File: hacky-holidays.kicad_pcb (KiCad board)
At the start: 2 copper layers, 96 x 96 mm, 39 parts, among them Q1 AO3401A, Q2 AO3400A, Q3 AO3400A, SW1 SW_Push, SW2 SW_Push, SW3 SW_Push, SW4 SW_SPDT, U1 TP4057, U2 CH552G, U3 DW01A

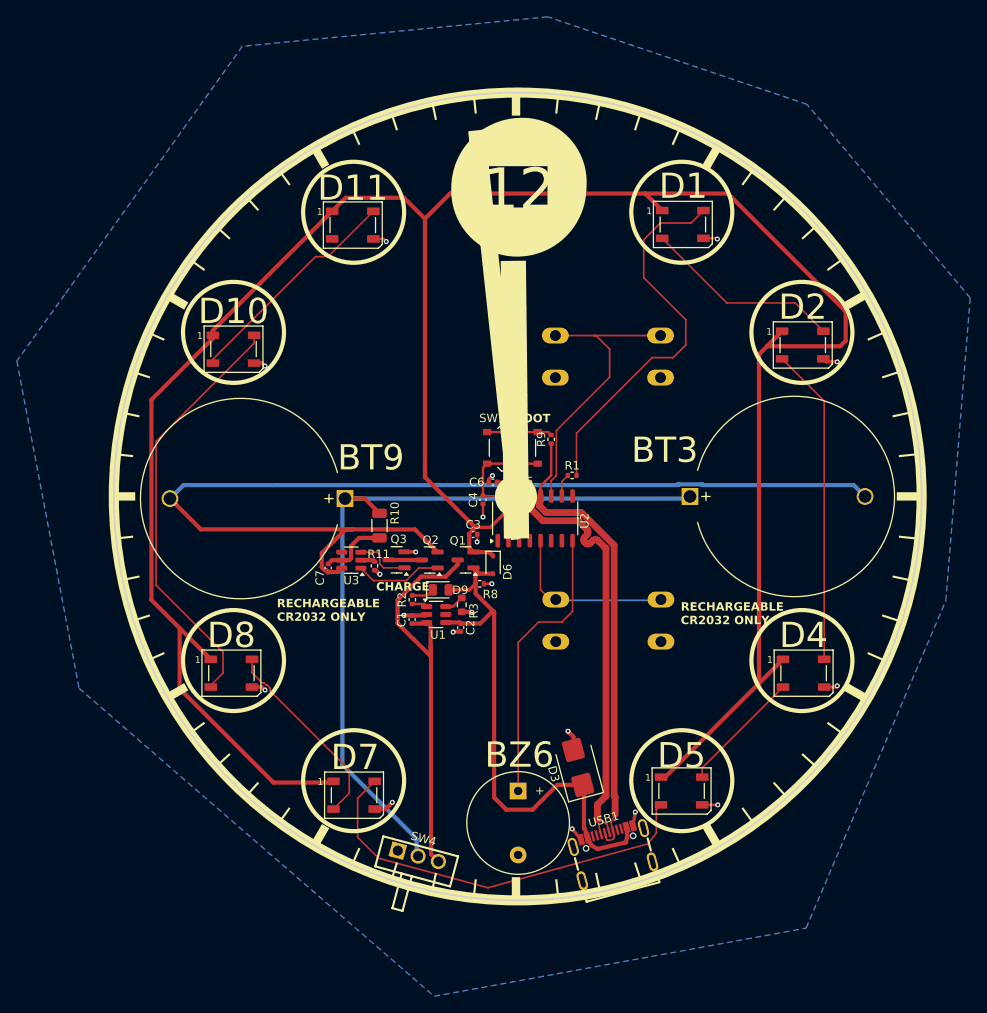
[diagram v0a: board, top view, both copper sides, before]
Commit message: update capacitor part numbers, add test pins, silkscreen updates
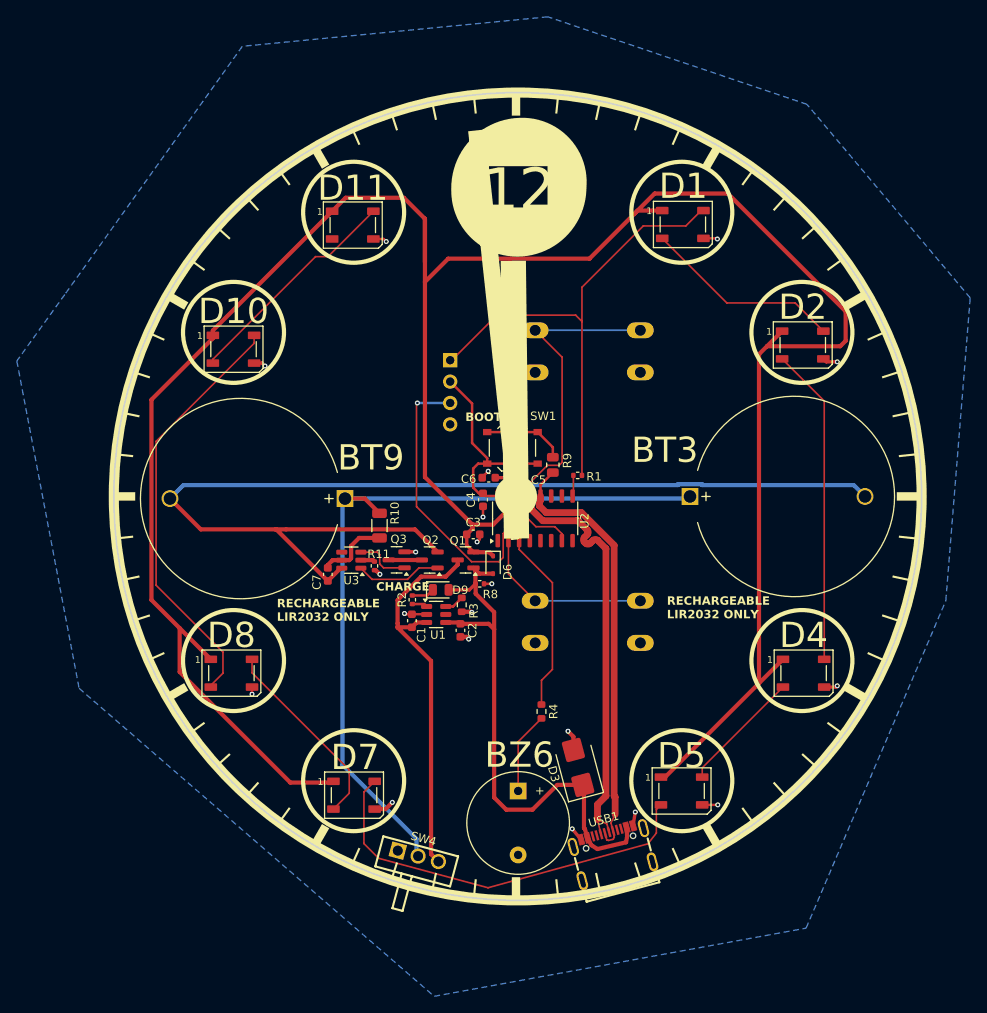
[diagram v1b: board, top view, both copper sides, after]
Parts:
- added J1: Conn_01x04_Pin, Connector_PinHeader_2.54mm:PinHeader_1x04_P2.54mm_Vertical, B.Cu at (199.0, 58.3)
- added QR*****: https://github.com/grimsteel/pixel-clock, custom-footprints:qrcode, B.Cu at (176.4, 75.0)
- added R4: 220, Resistor_SMD:R_0603_1608Metric, F.Cu at (209.8, 100.0)
- C1, C2, C3, C4, C5, C6, C7: footprint Capacitor_SMD:C_0402_1005Metric -> Capacitor_SMD:C_0603_1608Metric
- R9: footprint Resistor_SMD:R_0402_1005Metric -> Resistor_SMD:R_0805_2012Metric
- moved R9 3.05 mm to (211.2, 70.8)
- moved SW2 2.48 mm to (221.6, 54.8)
- moved SW3 2.45 mm to (221.6, 86.9)
- moved C7 0.77 mm to (184.5, 83.8)
- moved C6 0.73 mm to (203.6, 72.3)
- moved C5 0.71 mm to (206.6, 72.3)
- moved R1 0.65 mm to (214.2, 72.0)
- moved C2 0.34 mm to (200.2, 90.4)
- moved C1 0.15 mm to (194.4, 89.3)
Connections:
- BZ6 pad 1: BUZ -> Net-(BZ6-+)
- D1 pad 4: Net-(D1-DIN) -> WS2812B
- R1 pad 1: WS2812B -> Net-(U2-P1.1/T2EX/CAP2/TIN1/VBUS2/AIN0)
- R1 pad 2: Net-(D1-DIN) -> WS2812B
- U2 pad 10: WS2812B -> unconnected-(U2-P3.3/INT1-Pad10)
- U2 pad 11: BTN1 -> unconnected-(U2-P3.4/PWM2/RXD1_/T0-Pad11)
- U2 pad 2: unconnected-(U2-P1.4/T2_/CAP1_/SCS/TIN2/UCC1/AIN1-Pad2) -> BTN2
- U2 pad 3: unconnected-(U2-P1.5/MOSI/PWM1/TIN3/UCC2/AIN2-Pad3) -> BUZ
- U2 pad 5: BTN2 -> unconnected-(U2-P1.7/SCK/TXD1/TIN5-Pad5)
- U2 pad 7: unconnected-(U2-P3.1/PWM2_/TXD-Pad7) -> BTN1
- U2 pad 8: BUZ -> unconnected-(U2-P3.0/PWM1_/RXD-Pad8)
- U2 pad 9: unconnected-(U2-P1.1/T2EX/CAP2/TIN1/VBUS2/AIN0-Pad9) -> Net-(U2-P1.1/T2EX/CAP2/TIN1/VBUS2/AIN0)
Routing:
- net WS2812B: track 2.75 -> 58.7 mm
- net Net-(D1-DIN): track 45.5 -> 0.00 mm
- net BUZ: track 34.1 -> 56.9 mm, vias 0 -> 1
- net +3.3V: track 11.8 -> 25.1 mm
- net BTN1: track 35.4 -> 46.4 mm
- net Net-(BZ6-+): track 0.00 -> 9.77 mm
- net +5V: track 299.2 -> 307.9 mm
- net BATT: track 49.7 -> 46.2 mm
- net D+: track 55.6 -> 52.2 mm
- net Net-(U2-P1.1/T2EX/CAP2/TIN1/VBUS2/AIN0): track 0.00 -> 2.49 mm
- net Net-(R9-Pad2): track 7.74 -> 9.55 mm
- net -BATT: track 127.7 -> 129.5 mm
- net GND: track 34.3 -> 33.2 mm, vias 21 -> 22
- net VBUS: track 68.1 -> 67.1 mm
- net BTN2: track 20.1 -> 21.0 mm
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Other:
- board text added: "+3.3V"
- board text added: "BUZ"
- board text added: "GND"
- board text added: "NEO"
- board text added: "RECHARGEABLE LIR2032 ONLY"
- board text added: "github.com/grimsteel/pixel-clock"
- board text removed: "RECHARGEABLE CR2032 ONLY"

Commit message: tidy schematic
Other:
- board text added: "JLCJLCJLCJLC"
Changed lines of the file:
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@@
 		)
 		(property "Footprint" ""
-			(at 0 0 0)
-			(layer "B.Fab")
+			(at 0 0 180)
+			(layer "F.Fab")
 			(hide yes)
 			(effects
@@
 					(thickness 0.15)
 				)
-				(justify mirror)
 			)
 		)
@@
 		)
 	)
+	(gr_text "JLCJLCJLCJLC"
+		(at 227.37 83.85 0)
+		(layer "B.SilkS")
+		(effects
+			(font
+				(size 1 1)
+				(thickness 0.15)
+			)
+			(justify mirror)
+		)
+	)

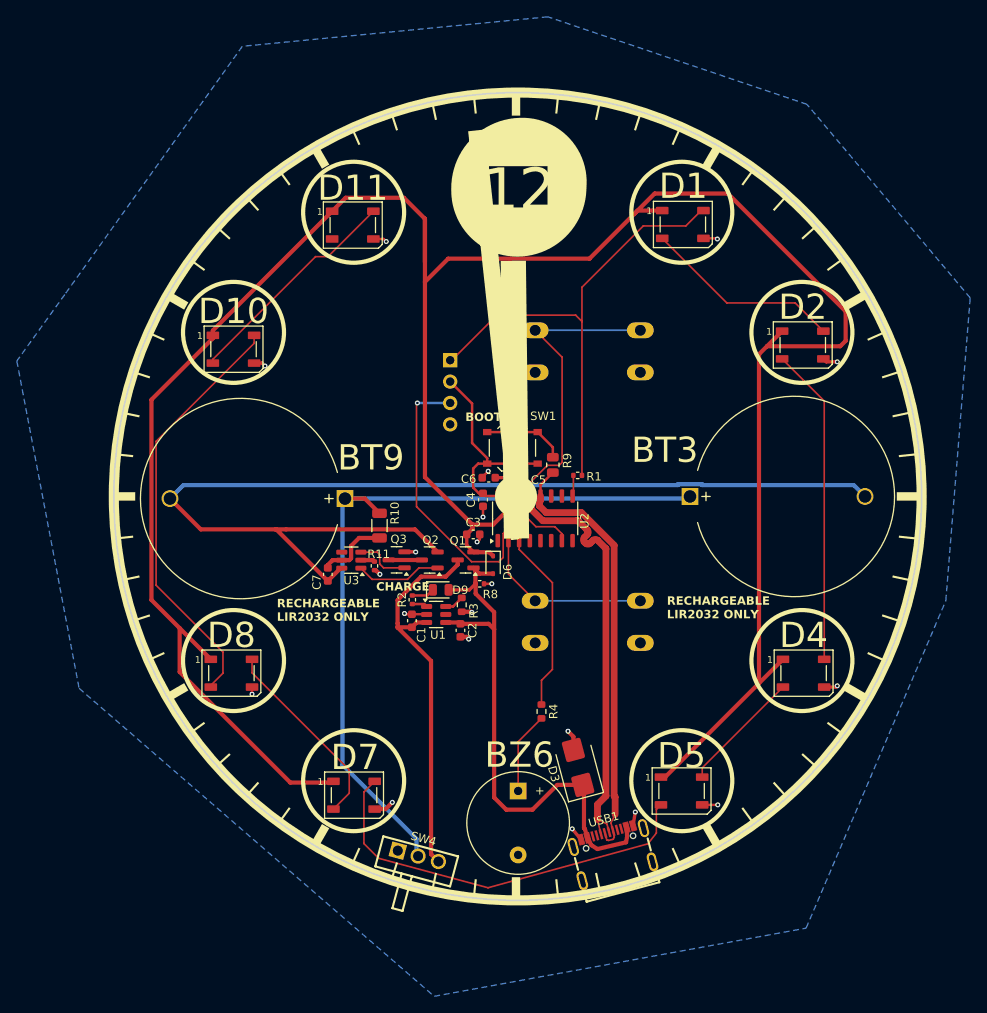
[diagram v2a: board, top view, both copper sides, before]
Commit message: add mounting hole
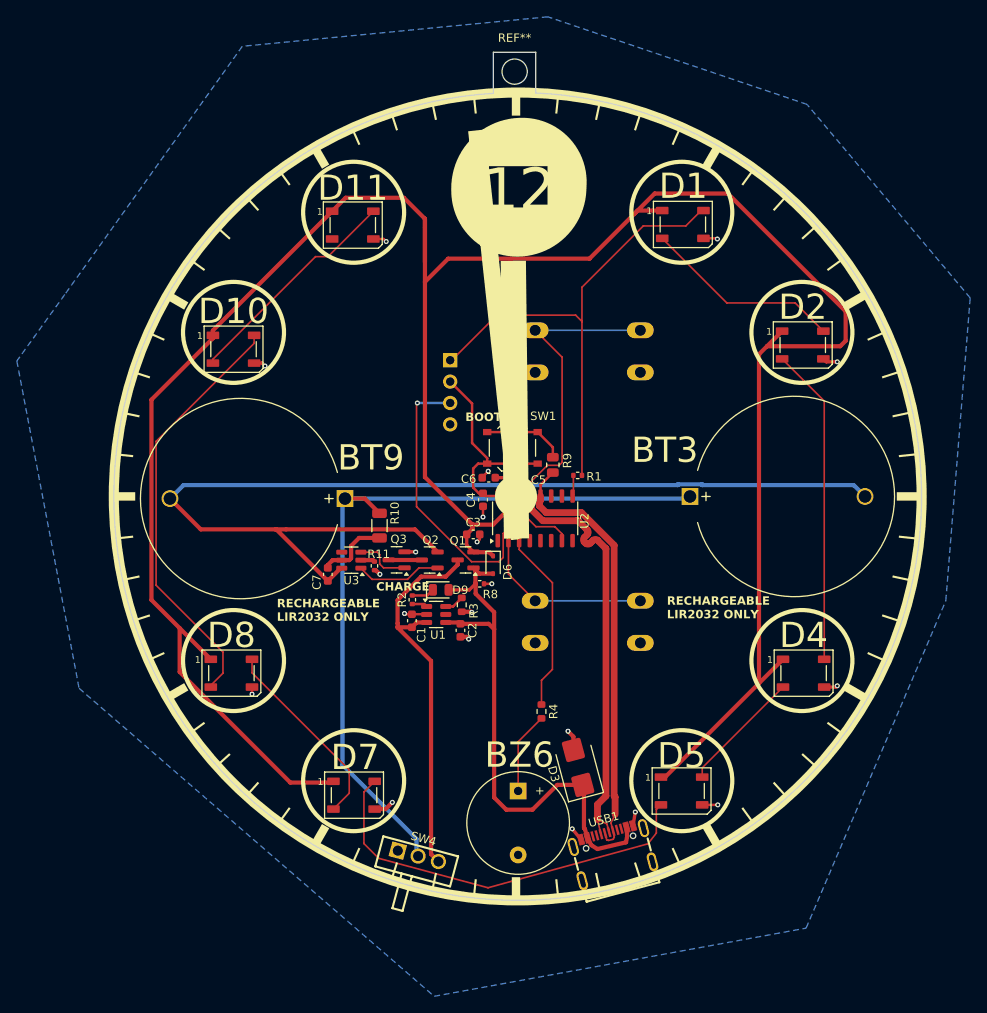
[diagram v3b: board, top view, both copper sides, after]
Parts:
- added REF**: MountingHole_3mm, MountingHole:MountingHole_3mm, F.Cu at (206.7, 24.0)
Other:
- board size 96 x 96 mm -> 96 x 100.8 mm
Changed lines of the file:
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@@
 		)
 	)
+	(footprint "MountingHole:MountingHole_3mm"
+		(layer "F.Cu")
+		(at 206.66 24.01)
+		(descr "Mounting Hole 3mm, no annular")
+		(tags "mounting hole 3mm no annular")
+		(property "Reference" "REF**"
+			(at 0 -4 0)
+			(layer "F.SilkS")
+			(effects
+				(font
+					(size 1 1)
+					(thickness 0.15)
+				)
+			)
+		)
+		(property "Value" "MountingHole_3mm"
+			(at 0 4 0)
+			(layer "F.Fab")
+			(effects
+				(font
+					(size 1 1)
+					(thickness 0.15)
+				)
+			)
+		)
+		(property "Footprint" ""
+			(at 0 0 0)
+			(layer "F.Fab")
+			(hide yes)
+			(effects
+				(font
+					(size 1.27 1.27)
+					(thickness 0.15)
+				)
+			)
+		)
+		(property "Datasheet" ""
+			(at 0 0 0)
+			(unlocked yes)
+			(layer "F.Fab")
+			(hide yes)
+			(effects
+				(font
+					(size 1.27 1.27)
+					(thickness 0.15)
+				)
+			)
+		)
+		(property "Description" ""
+			(at 0 0 0)
+			(unlocked yes)
+			(layer "F.Fab")
+			(hide yes)
+			(effects
+				(font
+					(size 1.27 1.27)
+					(thickness 0.15)
+				)
+			)
+		)
+		(attr exclude_from_pos_files exclude_from_bom)
+		(fp_circle
+			(center 0 0)
+			(end 3 0)
+			(stroke
+				(width 0.15)
+				(type solid)
+			)
+			(fill no)
+			(layer "Cmts.User")
+		)
+		(fp_circle
+			(center 0 0)
+			(end 3.25 0)
+			(stroke
+				(width 0.05)
+				(type solid)
+			)
+			(fill no)
+			(layer "F.CrtYd")
+		)
+		(fp_text user "${REFERENCE}"
+			(at 0 0 0)
+			(layer "F.Fab")
+			(effects
+				(font
+					(size 1 1)
+					(thickness 0.15)
+				)
+			)
+		)
+		(pad "" np_thru_hole circle
+			(at 0 0)
+			(size 3 3)
+			(drill 3)
+			(layers "*.Cu" "*.Mask")
+		)
+		(embedded_fonts no)
+	)
 	(footprint "LED_SMD:LED_WS2812B_PLCC4_5.0x5.0mm_P3.2mm"
 		(layer "F.Cu")
@@
 		(layer "Dwgs.User")
 	)
-	(gr_circle
-		(center 207.024991 74.5)
-		(end 255.024991 74.5)
+	(gr_line
+		(start 209.17 21.71)
+		(end 204.13 21.71)
 		(stroke
-			(width 0.2)
+			(width 0.05)
+			(type default)
+		)
+		(layer "Edge.Cuts")
+	)
+	(gr_line
+		(start 204.13 26.59)
+		(end 204.13 21.71)
+		(stroke
+			(width 0.05)
+			(type default)
+		)
+		(layer "Edge.Cuts")
+	)
+	(gr_arc
+		(start 209.168876 26.550518)
+		(mid 207.401062 122.495913)
+		(end 204.13 26.59)
+		(stroke
+			(width 0.05)
+			(type default)
+		)
+		(layer "Edge.Cuts")
+	)
+	(gr_line
+		(start 209.17 26.55)
+		(end 209.17 21.71)
+		(stroke
+			(width 0.05)
 			(type default)
 		)
-		(fill no)
 		(layer "Edge.Cuts")
 	)

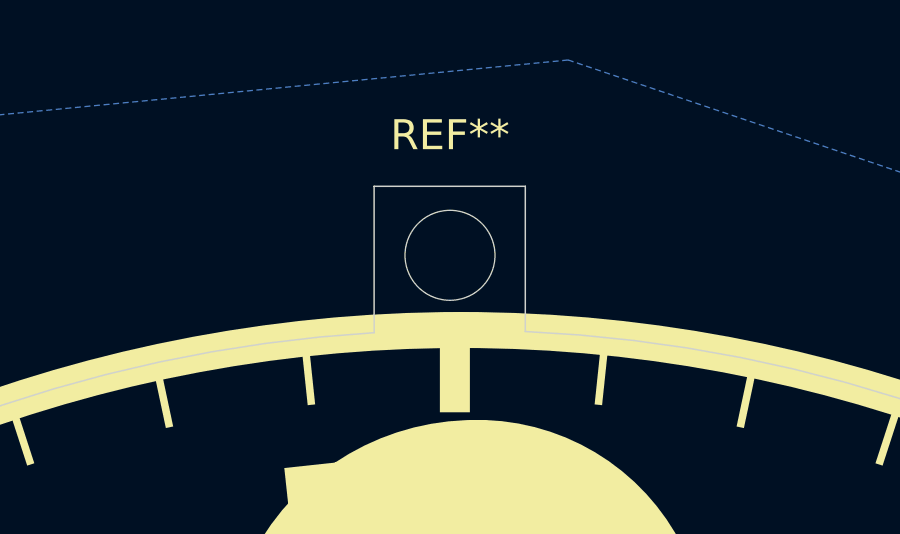
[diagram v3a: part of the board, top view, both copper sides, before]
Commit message: make pcb below 100x100
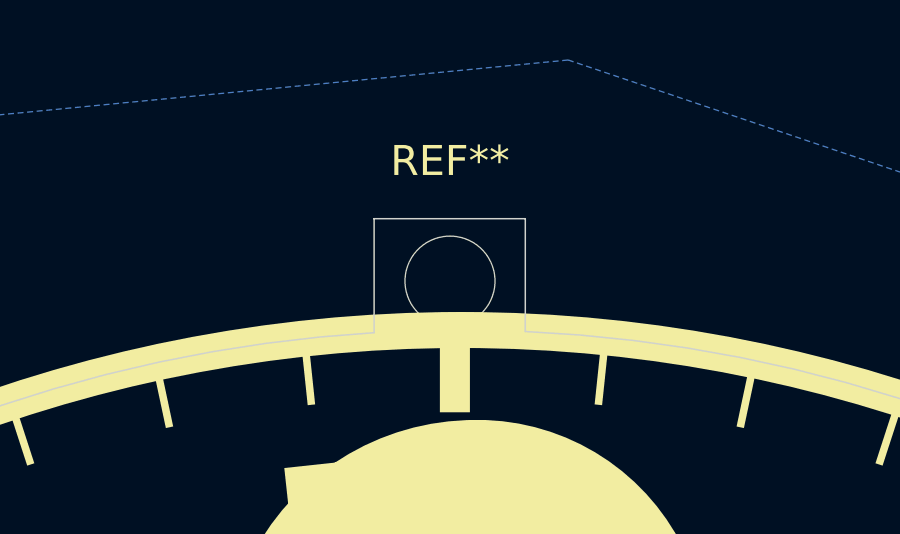
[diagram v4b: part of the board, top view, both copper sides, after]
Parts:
- moved REF** 0.86 mm to (206.7, 24.9)
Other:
- board size 96 x 100.8 mm -> 96 x 99.7 mm
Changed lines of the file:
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@@
 	(footprint "MountingHole:MountingHole_3mm"
 		(layer "F.Cu")
-		(at 206.66 24.01)
+		(at 206.66 24.87)
 		(descr "Mounting Hole 3mm, no annular")
 		(tags "mounting hole 3mm no annular")
@@
 	)
 	(gr_line
-		(start 209.17 21.71)
-		(end 204.13 21.71)
+		(start 209.17 22.79)
+		(end 204.13 22.79)
 		(stroke
 			(width 0.05)
@@
 	(gr_line
 		(start 204.13 26.59)
-		(end 204.13 21.71)
+		(end 204.13 22.79)
 		(stroke
 			(width 0.05)
@@
 	(gr_line
 		(start 209.17 26.55)
-		(end 209.17 21.71)
+		(end 209.17 22.79)
 		(stroke
 			(width 0.05)

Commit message: invert qr code
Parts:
- moved QR***** 0.51 mm to (175.9, 74.8)

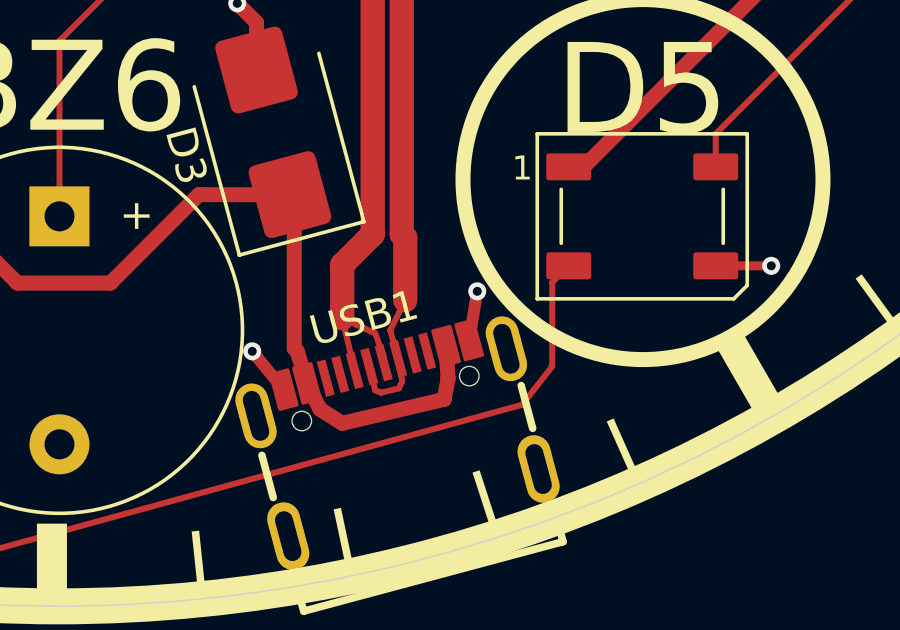
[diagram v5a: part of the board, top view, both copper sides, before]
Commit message: add usb cc resistors
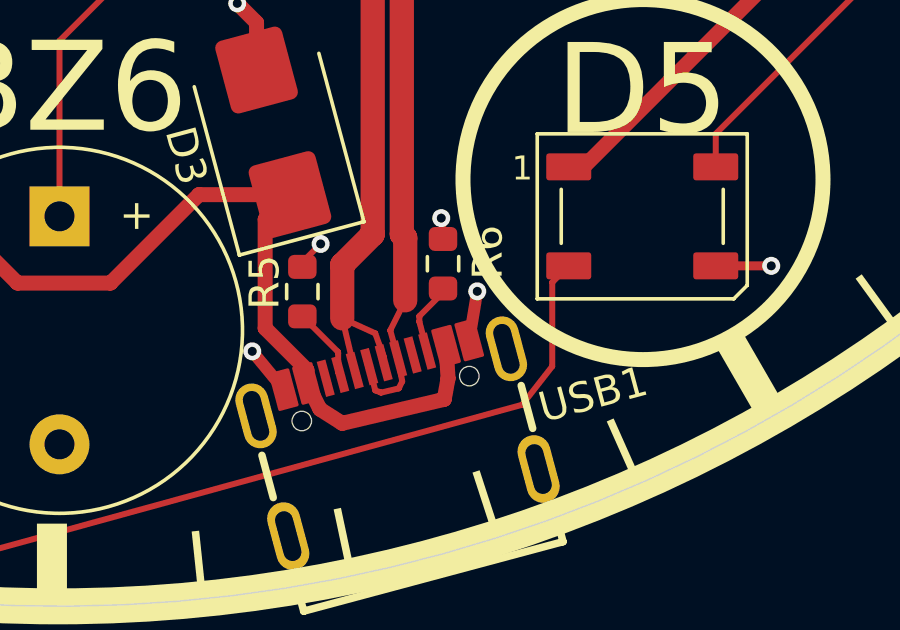
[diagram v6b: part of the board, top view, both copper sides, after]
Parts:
- added R5: 5.1K, Resistor_SMD:R_0603_1608Metric, F.Cu at (215.2, 112.0)
- added R6: 5.1K, Resistor_SMD:R_0603_1608Metric, F.Cu at (219.9, 111.1)
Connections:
- USB1 pad A5: unconnected-(USB1-CC1-PadA5) -> CC1
- USB1 pad B5: unconnected-(USB1-CC2-PadB5) -> CC2
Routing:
- net CC1: track 0.00 -> 2.46 mm
- net CC2: track 0.00 -> 2.45 mm
- net GND: track 33.2 -> 35.0 mm, vias 22 -> 24
- net VBUS: track 67.1 -> 67.8 mm
